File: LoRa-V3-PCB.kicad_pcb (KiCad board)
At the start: 2 copper layers, 62 x 50 mm, 85 parts, among them IC1 114993121, IC10 BR24G1MFVT-5AE2, IC11 BR24G1MFVT-5AE2, IC12 AEM00920, IC13 MCP73123T-22SI/MF, IC2 CP2102N-Axx-xQFN24, IC3 USBLC6-2P6, IC5 BME680, IC6 SHT40-BD1B-R2, IC7 TSL25911FN, IC8 BR24G1MFVT-5AE2, IC9 BR24G1MFVT-5AE2, Q1 PJC7400_R1_00001, Q2 Si2367DS, Q3 Si2367DS, Q4 Si2367DS, SW1 434331045822, SW2 SLLB510100

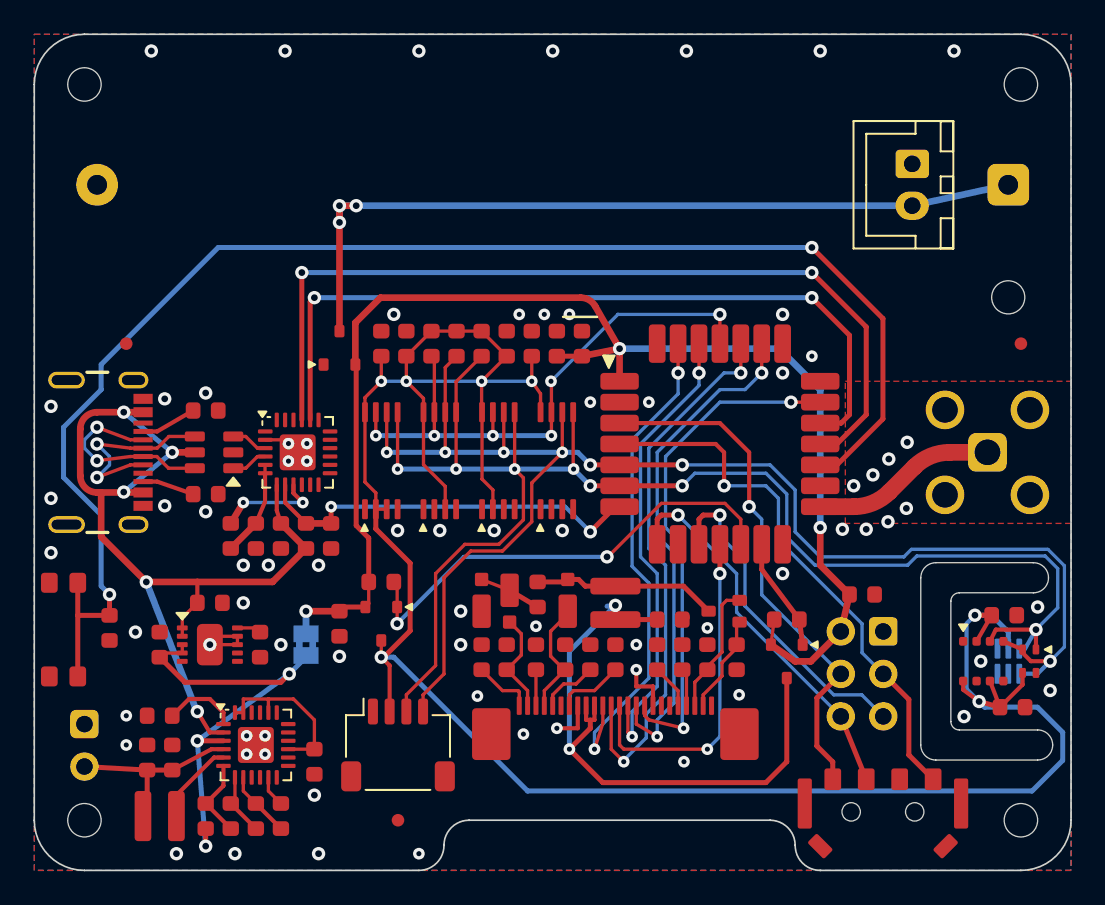
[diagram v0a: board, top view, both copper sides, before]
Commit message: fix DRC error
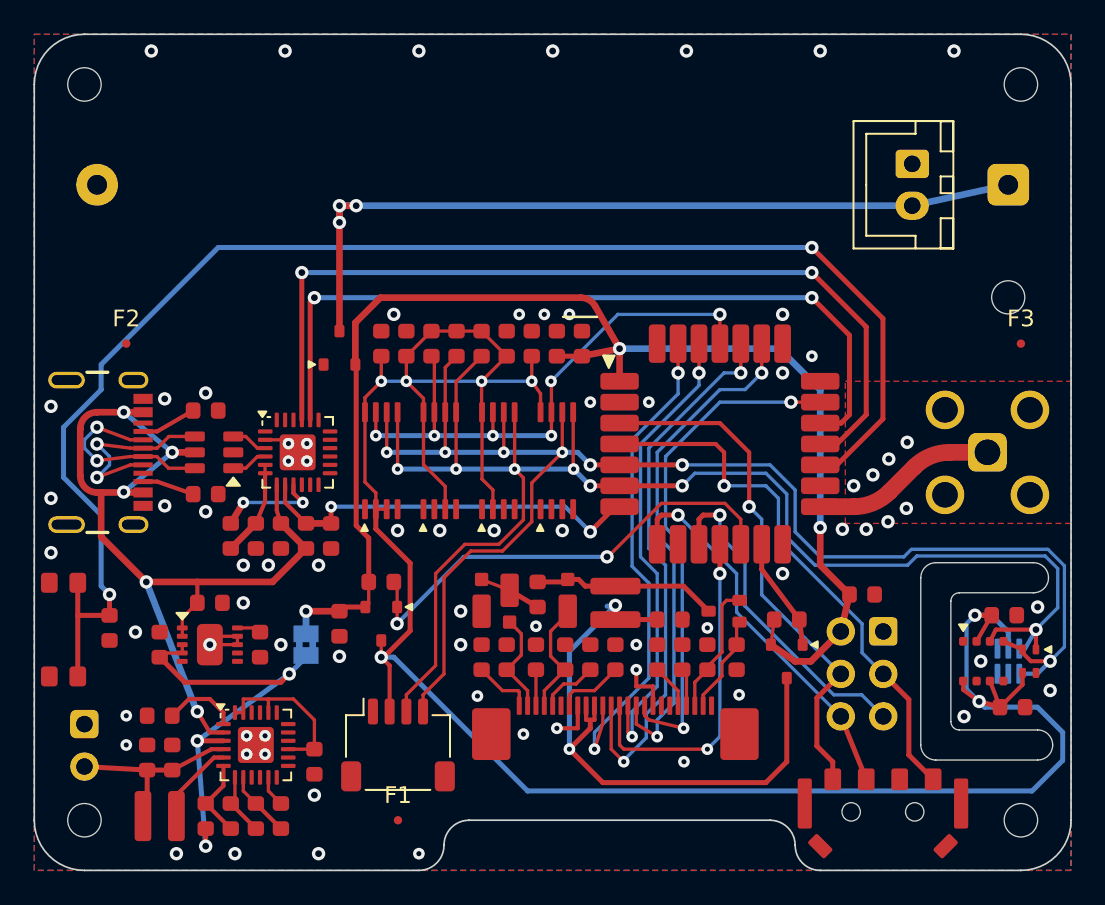
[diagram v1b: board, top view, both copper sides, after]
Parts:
- C1, C10, C11, C12, C13, C14, C15, C2, C20, C21, C22, C23, C24, C25, C3, C30, C31, C32, C33, C34, C35, C36, C37, C4, C5, C6, C7, C8: footprint 1GlobalFootprintsLibrary:C_0603_nominal -> 1projectLibrary:C_0603_nominal
- F1, F2, F3: footprint Fiducial:Fiducial_0.75mm_Mask1.5mm -> Fiducial:Fiducial_0.5mm_Mask1mm
- IC1: footprint 1GlobalFootprintsLibrary:LoRa-E5 -> 1projectLibrary:LoRa-E5
- R1, R10, R11, R12, R13, R14, R15, R16, R17, R18, R2, R3, R4, R5, R6, R7, R8, R9: footprint 1GlobalFootprintsLibrary:R_0603_nominal -> 1projectLibrary:R_0603_nominal
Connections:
- IC1 pad 9: UART1-RX -> unconnected-(IC1-PB7-Pad9)

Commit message: fix footprints
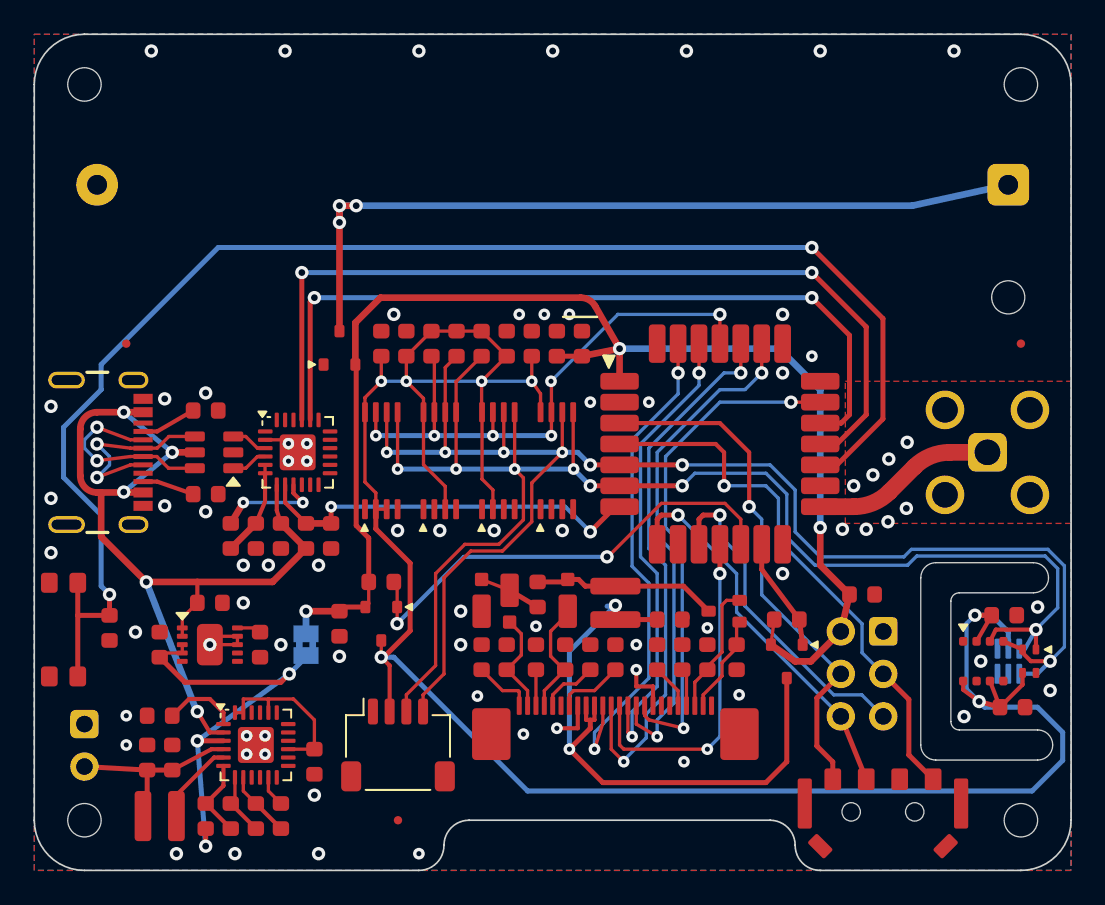
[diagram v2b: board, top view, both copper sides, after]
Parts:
- removed CONN3: B2B-XH-A(LF)(SN), 1projectLibrary:JST_XH_B2B-XH-A_1x02_P2.50mm_Vertical
- H1, H2: footprint 1projectLibrary:MountingHole_2mm -> 1projectLibrary:MountingHole_2mm_noCourtyard
- IC10, IC11, IC8, IC9: footprint 1GlobalFootprintsLibrary:BR24G1M-TSSOP-B8 -> 1projectLibrary:BR24G1M-TSSOP-B8
- Q2, Q3, Q4: footprint 1GlobalFootprintsLibrary:SI2367DS-SOT-23 -> 1projectLibrary:SI2367DS-SOT-23

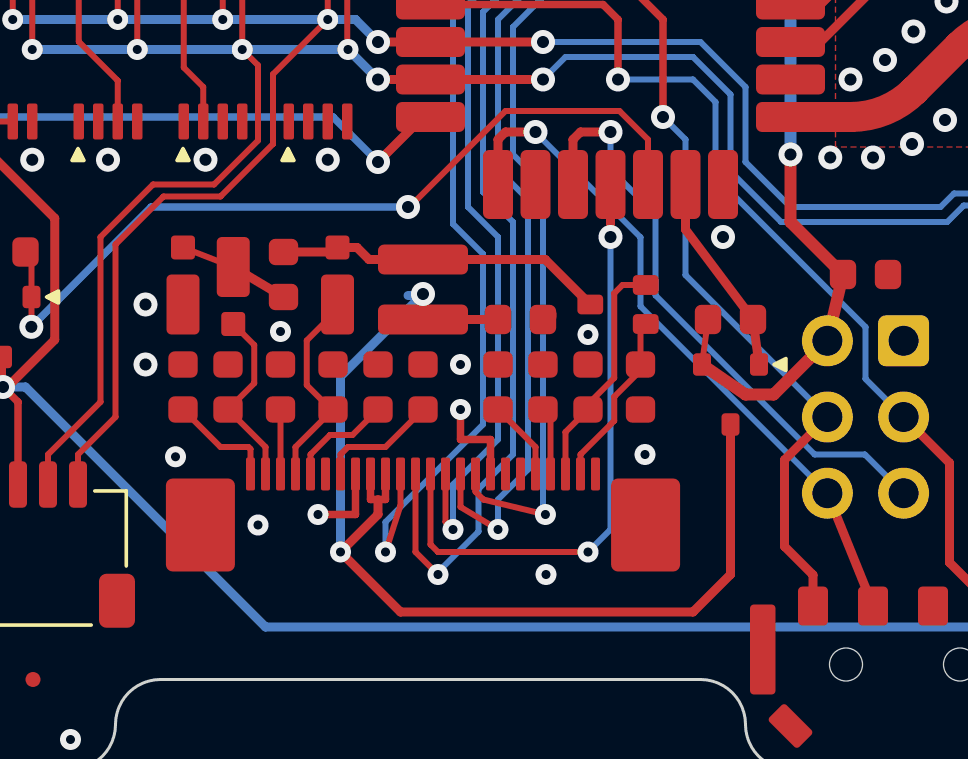
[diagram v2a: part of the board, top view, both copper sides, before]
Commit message: outcommented blender render
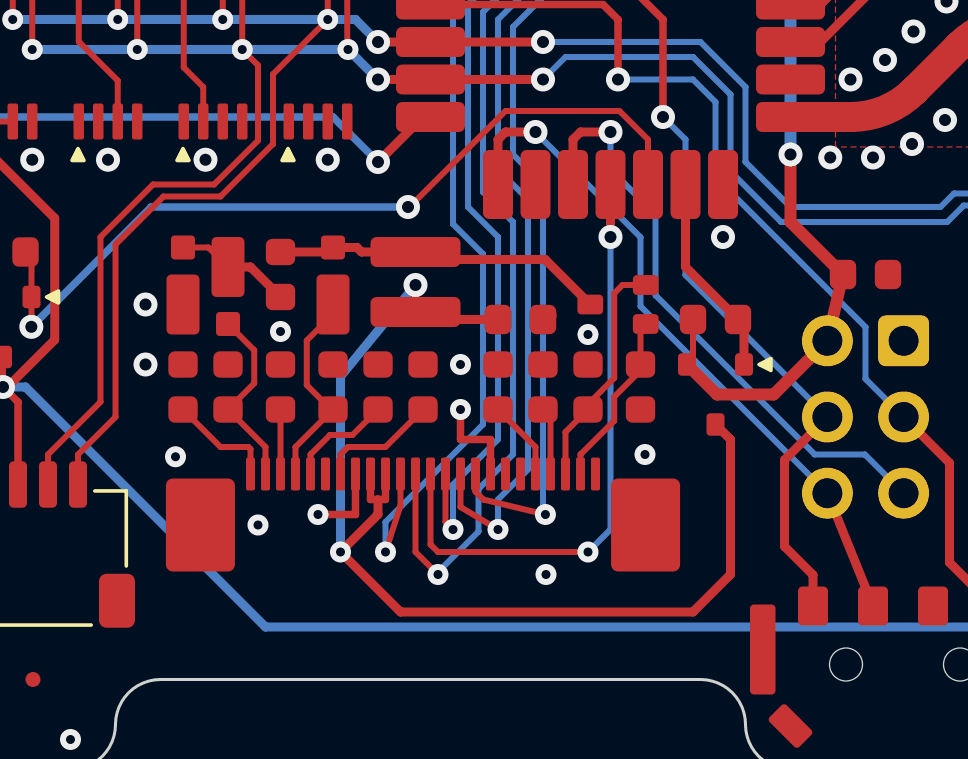
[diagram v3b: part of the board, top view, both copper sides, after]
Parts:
- moved Q2 0.50 mm to (158.5, 109.5)
- moved R17 0.50 mm to (158.5, 107.0)
- moved L1 0.35 mm to (148.5, 105.8)
- moved D1 0.18 mm to (142.2, 106.5)
- moved D2 0.15 mm to (145.8, 105.2)
- moved C15 0.10 mm to (144.0, 105.5)
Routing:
- net +3.3V: track 81.2 -> 81.9 mm
